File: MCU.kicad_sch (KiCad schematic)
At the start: 30 parts, among them J11 B5B-PH-K-S, J6 61300311121, J7 ARM Cortex Debug, J8 B7B-PH-K-S, J9 USB_C, U4 STM32F446RET6TR, U6 USBLC6-4SC6-EV, Y1 8MHz

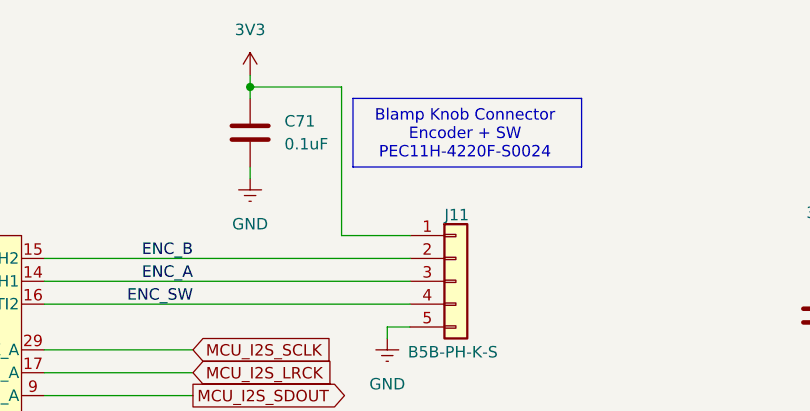
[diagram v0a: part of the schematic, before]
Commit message: Remove bypass cap for encoder, shouldn't need it
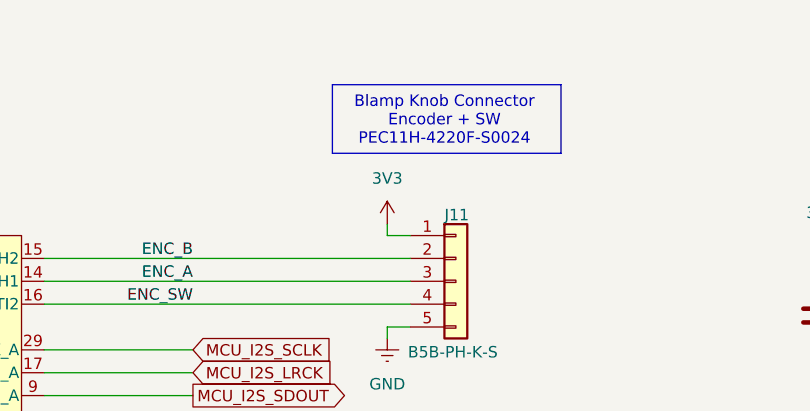
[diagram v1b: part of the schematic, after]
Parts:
- removed C71: 0.1uF, symbol Device:C
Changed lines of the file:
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@@
 	)
 	(rectangle
-		(start 198.12 30.48)
-		(end 223.52 38.1)
+		(start 195.834 28.956)
+		(end 221.234 36.576)
 		(stroke
 			(width 0)
@@
 	(text "Blamp Knob Connector\nEncoder + SW\nPEC11H-4220F-S0024\n"
 		(exclude_from_sim no)
-		(at 210.566 34.544 0)
+		(at 208.28 33.02 0)
 		(effects
 			(font
@@
 	)
 	(junction
-		(at 186.69 29.21)
-		(diameter 0)
-		(color 0 0 0 0)
-	)
-	(junction
 		(at 92.71 46.99)
 		(diameter 0)
@@
 	(wire
 		(pts
-			(xy 186.69 38.1) (xy 186.69 39.37)
-		)
-		(stroke
-			(width 0)
-			(type default)
-		)
-	)
-	(wire
-		(pts
 			(xy 105.41 31.75) (xy 105.41 33.02)
 		)
@@
 	(wire
 		(pts
-			(xy 186.69 29.21) (xy 196.85 29.21)
-		)
-		(stroke
-			(width 0)
-			(type default)
-		)
-	)
-	(wire
-		(pts
 			(xy 260.35 130.81) (xy 250.19 130.81)
 		)
@@
 	(wire
 		(pts
-			(xy 186.69 29.21) (xy 186.69 30.48)
-		)
-		(stroke
-			(width 0)
-			(type default)
-		)
-	)
-	(wire
-		(pts
 			(xy 163.83 93.98) (xy 219.71 93.98)
 		)
@@
 	(wire
 		(pts
-			(xy 196.85 45.72) (xy 204.47 45.72)
+			(xy 201.93 45.72) (xy 204.47 45.72)
 		)
 		(stroke
@@
 	(wire
 		(pts
-			(xy 196.85 45.72) (xy 196.85 29.21)
-		)
-		(stroke
-			(width 0)
-			(type default)
-		)
-	)
-	(wire
-		(pts
-			(xy 186.69 27.94) (xy 186.69 29.21)
+			(xy 201.93 44.45) (xy 201.93 45.72)
 		)
 		(stroke
@@
 	)
 	(symbol
-		(lib_id "power:GNDREF")
-		(at 186.69 39.37 0)
-		(unit 1)
-		(body_style 1)
-		(exclude_from_sim no)
-		(in_bom yes)
-		(on_board yes)
-		(in_pos_files yes)
-		(dnp no)
-		(fields_autoplaced yes)
-		(property "Reference" "#PWR0108"
-			(at 186.69 45.72 0)
-			(hide yes)
-			(show_name no)
-			(do_not_autoplace no)
-			(effects
-				(font
-					(size 1.27 1.27)
-				)
-			)
-		)
-		(property "Value" "GND"
-			(at 186.69 44.45 0)
-			(show_name no)
-			(do_not_autoplace no)
-			(effects
-				(font
-					(size 1.27 1.27)
-				)
-			)
-		)
-		(property "Footprint" ""
-			(at 186.69 39.37 0)
-			(hide yes)
-			(show_name no)
-			(do_not_autoplace no)
-			(effects
-				(font
-					(size 1.27 1.27)
-				)
-			)
-		)
-		(property "Datasheet" ""
-			(at 186.69 39.37 0)
-			(hide yes)
-			(show_name no)
-			(do_not_autoplace no)
-			(effects
-				(font
-					(size 1.27 1.27)
-				)
-			)
-		)
-		(property "Description" "Power symbol creates a global label with name \"GNDREF\" , reference supply ground"
-			(at 186.69 39.37 0)
-			(hide yes)
-			(show_name no)
-			(do_not_autoplace no)
-			(effects
-				(font
-					(size 1.27 1.27)
-				)
-			)
-		)
-		(pin "1"
-		)
-		(instances
-			(project "Blamp"
-				(path "/90f900ff-e6f7-4b42-9414-7e4ea0d3c559/56106df7-956a-4c94-981d-a3f2f405ebf9"
-					(reference "#PWR0108")
-					(unit 1)
-				)
-			)
-		)
-	)
-	(symbol
 		(lib_id "Device:R_US")
 		(at 198.12 111.76 180)
@@
 	)
 	(symbol
-		(lib_id "Device:C")
-		(at 186.69 34.29 0)
-		(unit 1)
-		(body_style 1)
-		(exclude_from_sim no)
-		(in_bom yes)
-		(on_board yes)
-		(in_pos_files yes)
-		(dnp no)
-		(property "Reference" "C71"
-			(at 190.5 33.0199 0)
-			(show_name no)
-			(do_not_autoplace no)
-			(effects
-				(font
-					(size 1.27 1.27)
-				)
-				(justify left)
-			)
-		)
-		(property "Value" "0.1uF"
-			(at 190.5 35.5599 0)
-			(show_name no)
-			(do_not_autoplace no)
-			(effects
-				(font
-					(size 1.27 1.27)
-				)
-				(justify left)
-			)
-		)
-		(property "Footprint" ""
-			(at 187.6552 38.1 0)
-			(hide yes)
-			(show_name no)
-			(do_not_autoplace no)
-			(effects
-				(font
-					(size 1.27 1.27)
-				)
-			)
-		)
-		(property "Datasheet" ""
-			(at 186.69 34.29 0)
-			(hide yes)
-			(show_name no)
-			(do_not_autoplace no)
-			(effects
-				(font
-					(size 1.27 1.27)
-				)
-			)
-		)
-		(property "Description" "Unpolarized capacitor"
-			(at 186.69 34.29 0)
-			(hide yes)
-			(show_name no)
-			(do_not_autoplace no)
-			(effects
-				(font
-					(size 1.27 1.27)
-				)
-			)
-		)
-		(pin "1"
-		)
-		(pin "2"
-		)
-		(instances
-			(project "Blamp"
-				(path "/90f900ff-e6f7-4b42-9414-7e4ea0d3c559/56106df7-956a-4c94-981d-a3f2f405ebf9"
-					(reference "C71")
-					(unit 1)
-				)
-			)
-		)
-	)
-	(symbol
 		(lib_id "power:+5V")
-		(at 186.69 27.94 0)
+		(at 201.93 44.45 0)
 		(unit 1)
 		(body_style 1)
@@
 		(fields_autoplaced yes)
 		(property "Reference" "#PWR0105"
-			(at 186.69 31.75 0)
+			(at 201.93 48.26 0)
 			(hide yes)
 			(show_name no)
@@
 		)
 		(property "Value" "3V3"
-			(at 186.69 22.86 0)
+			(at 201.93 39.37 0)
 			(show_name no)
 			(do_not_autoplace no)
@@
 		)
 		(property "Footprint" ""
-			(at 186.69 27.94 0)
+			(at 201.93 44.45 0)
 			(hide yes)
 			(show_name no)
@@
 		)
 		(property "Datasheet" ""
-			(at 186.69 27.94 0)
+			(at 201.93 44.45 0)
 			(hide yes)
 			(show_name no)
@@
 		)
 		(property "Description" "Power symbol creates a global label with name \"+5V\""
-			(at 186.69 27.94 0)
+			(at 201.93 44.45 0)
 			(hide yes)
 			(show_name no)

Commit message: Add TP1,2 for I2C. Add 0 ohm for 5V to BT module
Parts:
- added TP1: MCU_I2C_SCL, Connector_Pin:Pin_D1.0mm_L10.0mm, symbol Connector:TestPoint
- added TP2: MCU_I2C_SDA, Connector_Pin:Pin_D1.0mm_L10.0mm, symbol Connector:TestPoint
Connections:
- net MCU_I2C_SCL: now also TP1.1
- net MCU_I2C_SDA: now also TP2.1
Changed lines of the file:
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@@
 	)
 	(junction
+		(at 66.0399 121.92)
+		(diameter 0)
+		(color 0 0 0 0)
+	)
+	(junction
 		(at 224.79 83.82)
 		(diameter 0)
@@
 	)
 	(junction
+		(at 66.04 119.38)
+		(diameter 0)
+		(color 0 0 0 0)
+	)
+	(junction
 		(at 111.76 52.07)
 		(diameter 0)
@@
 	(wire
 		(pts
-			(xy 59.69 121.92) (xy 113.03 121.92)
+			(xy 59.69 121.92) (xy 66.0399 121.92)
 		)
 		(stroke
@@
 	(wire
 		(pts
+			(xy 66.04 119.38) (xy 50.8 119.38)
+		)
+		(stroke
+			(width 0)
+			(type default)
+		)
+	)
+	(wire
+		(pts
 			(xy 67.31 46.99) (xy 73.66 46.99)
 		)
@@
 	(wire
 		(pts
-			(xy 113.03 119.38) (xy 50.8 119.38)
+			(xy 113.03 119.38) (xy 66.04 119.38)
 		)
 		(stroke
@@
 	(wire
 		(pts
+			(xy 66.0399 121.92) (xy 113.03 121.92)
+		)
+		(stroke
+			(width 0)
+			(type default)
+		)
+	)
+	(wire
+		(pts
 			(xy 62.23 35.56) (xy 62.23 33.02)
 		)
@@
 	)
 	(symbol
+		(lib_id "Connector:TestPoint")
+		(at 66.0399 121.92 0)
+		(mirror x)
+		(unit 1)
+		(body_style 1)
+		(exclude_from_sim no)
+		(in_bom yes)
+		(on_board yes)
+		(in_pos_files yes)
+		(dnp no)
+		(property "Reference" "TP2"
+			(at 67.3099 125.222 0)
+			(show_name no)
+			(do_not_autoplace no)
+			(effects
+				(font
+					(size 1.27 1.27)
+				)
+				(justify left)
+			)
+		)
+		(property "Value" "MCU_I2C_SDA"
+			(at 66.5479 123.19 0)
+			(show_name no)
+			(do_not_autoplace no)
+			(effects
+				(font
+					(size 1.27 1.27)
+				)
+				(justify left)
+			)
+		)
+		(property "Footprint" "Connector_Pin:Pin_D1.0mm_L10.0mm"
+			(at 71.1199 121.92 0)
+			(hide yes)
+			(show_name no)
+			(do_not_autoplace no)
+			(effects
+				(font
+					(size 1.27 1.27)
+				)
+			)
+		)
+		(property "Datasheet" ""
+			(at 71.1199 121.92 0)
+			(hide yes)
+			(show_name no)
+			(do_not_autoplace no)
+			(effects
+				(font
+					(size 1.27 1.27)
+				)
+			)
+		)
+		(property "Description" "test point"
+			(at 66.0399 121.92 0)
+			(hide yes)
+			(show_name no)
+			(do_not_autoplace no)
+			(effects
+				(font
+					(size 1.27 1.27)
+				)
+			)
+		)
+		(pin "1"
+		)
+		(instances
+			(project "Blamp"
+				(path "/90f900ff-e6f7-4b42-9414-7e4ea0d3c559/56106df7-956a-4c94-981d-a3f2f405ebf9"
+					(reference "TP2")
+					(unit 1)
+				)
+			)
+		)
+	)
+	(symbol
 		(lib_id "Device:C")
 		(at 86.36 39.37 0)
@@
 					(unit 1)
 				)
+			)
+		)
+	)
+	(symbol
+		(lib_id "Connector:TestPoint")
+		(at 66.04 119.38 0)
+		(unit 1)
+		(body_style 1)
+		(exclude_from_sim no)
+		(in_bom yes)
+		(on_board yes)
+		(in_pos_files yes)
+		(dnp no)
+		(property "Reference" "TP1"
+			(at 67.31 116.078 0)
+			(show_name no)
+			(do_not_autoplace no)
+			(effects
+				(font
+					(size 1.27 1.27)
+				)
+				(justify left)
+			)
+		)
+		(property "Value" "MCU_I2C_SCL"
+			(at 66.548 118.11 0)
+			(show_name no)
+			(do_not_autoplace no)
+			(effects
+				(font
+					(size 1.27 1.27)
+				)
+				(justify left)
+			)
+		)
+		(property "Footprint" "Connector_Pin:Pin_D1.0mm_L10.0mm"
+			(at 71.12 119.38 0)
+			(hide yes)
+			(show_name no)
+			(do_not_autoplace no)
+			(effects
+				(font
+					(size 1.27 1.27)
+				)
+			)
+		)
+		(property "Datasheet" ""
+			(at 71.12 119.38 0)
+			(hide yes)
+			(show_name no)
+			(do_not_autoplace no)
+			(effects
+				(font
+					(size 1.27 1.27)
+				)
+			)
+		)
+		(property "Description" "test point"
+			(at 66.04 119.38 0)
+			(hide yes)
+			(show_name no)
+			(do_not_autoplace no)
+			(effects
+				(font
+					(size 1.27 1.27)
+				)
+			)
+		)
+		(pin "1"
+		)
+		(instances
+			(project "Blamp"
+				(path "/90f900ff-e6f7-4b42-9414-7e4ea0d3c559/56106df7-956a-4c94-981d-a3f2f405ebf9"
+					(reference "TP1")
+					(unit 1)
+				)
